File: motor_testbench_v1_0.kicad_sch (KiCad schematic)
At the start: 32 parts, among them IC1 PJA3402_R1_00001, J1 USB_C_Receptacle_USB2.0_16P, J2 Conn_01x22_Pin, J3 Conn_01x05_Pin, J4 Conn_01x01_Pin, J5 Conn_01x01_Pin, U1 ESP32-S3-WROOM-2, U2 ESP32-S3-DevKitC

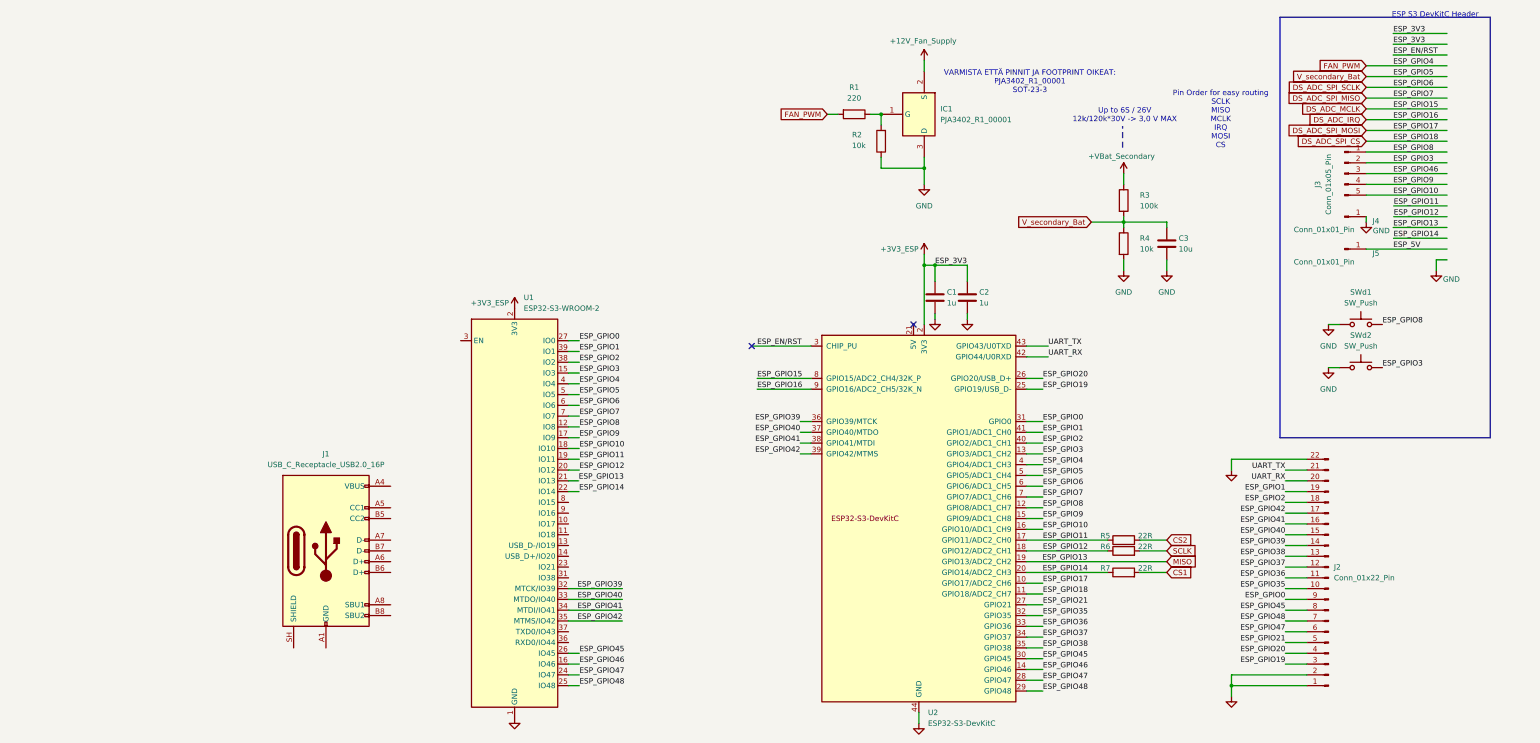
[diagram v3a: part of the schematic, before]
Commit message: Continue implementing ESP32 module
[KiCad Version: 10.0.3]
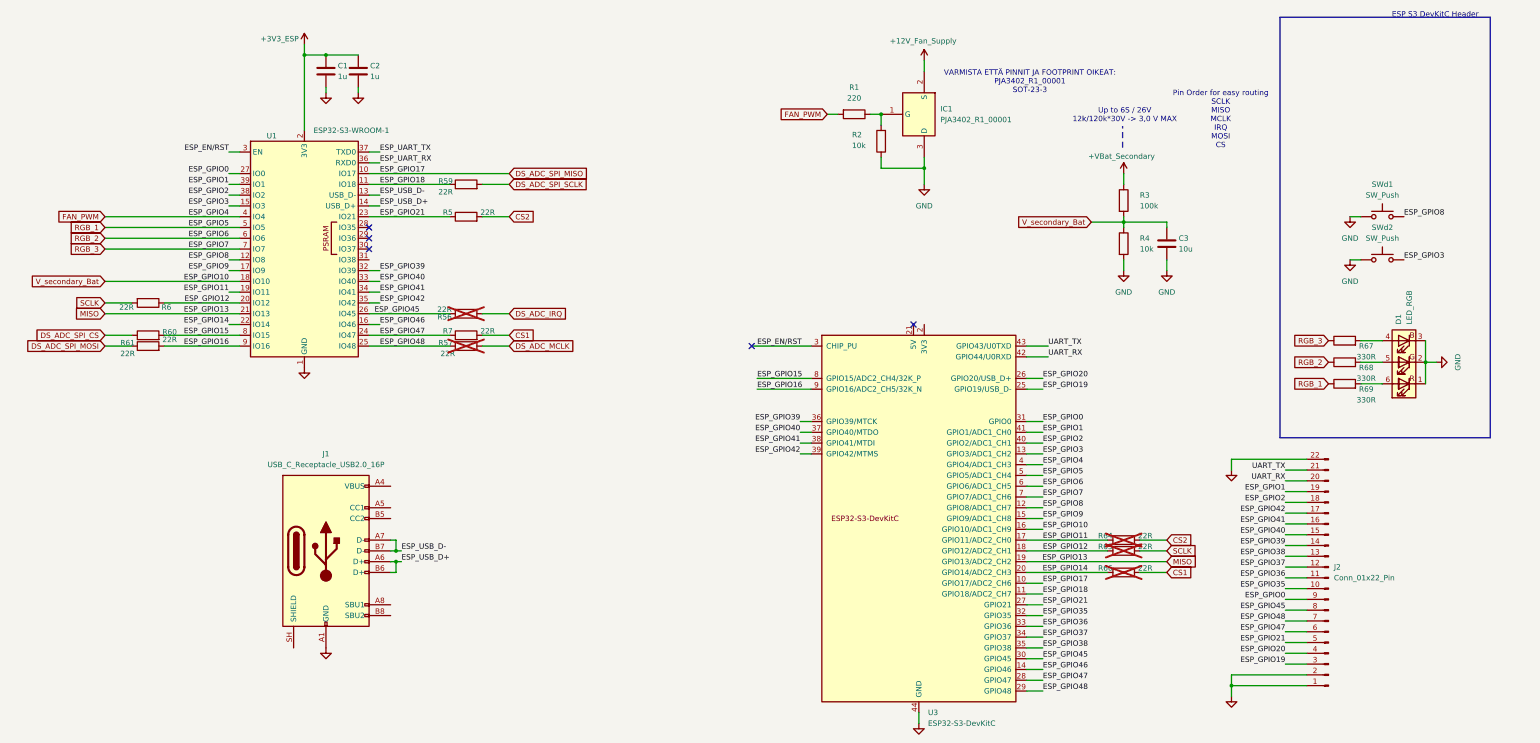
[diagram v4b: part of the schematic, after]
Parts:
- removed J3: Conn_01x05_Pin, Connector_PinHeader_2.54mm:PinHeader_1x05_P2.54mm_Vertical, symbol Connector:Conn_01x05_Pin
- removed J4, J5: Conn_01x01_Pin, Connector_PinHeader_2.54mm:PinHeader_1x01_P2.54mm_Vertical, symbol Connector:Conn_01x01_Pin
- removed U1: ESP32-S3-WROOM-2, RF_Module:ESP32-S3-WROOM-2, symbol RF_Module:ESP32-S3-WROOM-2
- added D1: LED_RGB, LED_SMD:LED_RGB_PLCC-6, symbol Device:LED_RGB
- added R56, R57, R59, R60, R61, R64, R65, R66: 22R, Resistor_SMD:R_0603_1608Metric_Pad0.98x0.95mm_HandSolder, symbol Device:R
- added R67, R68, R69: 330R, Resistor_SMD:R_0603_1608Metric_Pad0.98x0.95mm_HandSolder, symbol Device:R
- added U1: ESP32-S3-WROOM-1, RF_Module:ESP32-S3-WROOM-1, symbol RF_Module:ESP32-S3-WROOM-1
- renumbered U2 to U3
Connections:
- net ESP_GPIO10 is gone; now on net V_secondary_Bat: U3.16 (GPIO10/ADC1_CH9)
- net +3V3_ESP: now also U1.2 (3V3); no longer U3.1 (3V3), U3.2 (3V3)
- net CS1: now also R66.2
- net CS2: now also R64.2
- net DS_ADC_IRQ: now also R56.1; no longer U3.9 (GPIO16/ADC2_CH5/32K_N)
- net DS_ADC_MCLK: now also R57.2; no longer U3.8 (GPIO15/ADC2_CH4/32K_P)
- net DS_ADC_SPI_CS: now also R60.1; no longer U3.11 (GPIO18/ADC2_CH7)
- net DS_ADC_SPI_MISO: now also U3.10 (GPIO17/ADC2_CH6), U1.10 (IO17); no longer U3.7 (GPIO7/ADC1_CH6)
- net DS_ADC_SPI_MOSI: now also R61.1; no longer U3.10 (GPIO17/ADC2_CH6)
- net DS_ADC_SPI_SCLK: now also R59.2; no longer U3.6 (GPIO6/ADC1_CH5)
- net ESP_EN/RST: now also U1.3 (EN)
- net ESP_GPIO0: now also U1.27 (IO0)
- net ESP_GPIO1: now also U1.39 (IO1)
- net ESP_GPIO11: now also R64.1, U1.19 (IO11); no longer R5.1
- net ESP_GPIO12: now also R65.1, U1.20 (IO12)
- net ESP_GPIO14: now also R66.1, U1.22 (IO14); no longer R7.1
- net ESP_GPIO2: now also U1.38 (IO2)
- net ESP_GPIO21: now also R5.1, U1.23 (IO21)
- net ESP_GPIO3: now also U1.15 (IO3)
- net ESP_GPIO39: now also U1.32 (IO39)
- net ESP_GPIO40: now also U1.33 (IO40)
- net ESP_GPIO41: now also U1.34 (IO41)
- net ESP_GPIO42: now also U1.35 (IO42)
- net ESP_GPIO45: now also R56.2, U1.26 (IO45)
- net ESP_GPIO46: now also U1.16 (IO46)
- net ESP_GPIO47: now also R7.1, U1.24 (IO47)
- net ESP_GPIO48: now also R57.1, U1.25 (IO48)
- net ESP_GPIO8: now also U1.12 (IO8)
- net ESP_GPIO9: now also U1.17 (IO9)
- net FAN_PWM: now also U1.4 (IO4)
- net GND: now also J1.A1 (GND), J1.A12 (GND), J1.B1 (GND), J1.B12 (GND), D1.1 (RK), D1.2 (GK), D1.3 (BK), U1.1 (GND), U1.40 (GND), U1.41 (GND)
- net MISO: now also U1.21 (IO13)
- net SCLK: now also R65.2
- net V_secondary_Bat: now also U1.18 (IO10); no longer U3.5 (GPIO5/ADC1_CH4)
- net ESP_USB_D+: now reaches J1.A6 (D+)
- net ESP_USB_D+: now also J1.B6 (D+), U1.14 (USB_D+)
- net ESP_USB_D-: now reaches J1.A7 (D-)
- net ESP_USB_D-: now also J1.B7 (D-), U1.13 (USB_D-)
- new net: D1.6 (RA), R69.2
- new net: D1.5 (GA), R68.2
- new net: D1.4 (BA), R67.2
- new net: U3.1 (3V3), U3.2 (3V3)
- new net ESP_GPIO15: R60.2, U1.8 (IO15), U3.8 (GPIO15/ADC2_CH4/32K_P)
- new net ESP_GPIO16: R61.2, U1.9 (IO16), U3.9 (GPIO16/ADC2_CH5/32K_N)
- new net ESP_GPIO18: R59.1, U1.11 (IO18), U3.11 (GPIO18/ADC2_CH7)
- new net ESP_UART_RX: U1.36 (RXD0)
- new net ESP_UART_TX: U1.37 (TXD0)
- new net RGB_1: R69.1, U1.5 (IO5), U3.5 (GPIO5/ADC1_CH4)
- new net RGB_2: R68.1, U1.6 (IO6), U3.6 (GPIO6/ADC1_CH5)
- new net RGB_3: R67.1, U1.7 (IO7), U3.7 (GPIO7/ADC1_CH6)
- no-connect marks 2 -> 5
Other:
- moved on the sheet: SWd1, SWd2

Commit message: Add new GPIO header. Minor improvements.
[KiCad Version: 10.0.3]
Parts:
- removed J2: Conn_01x22_Pin, Connector_PinHeader_2.54mm:PinHeader_1x22_P2.54mm_Vertical, symbol Connector:Conn_01x22_Pin
- added J3: Conn_02x06_Odd_Even, Connector_PinHeader_2.00mm:PinHeader_2x06_P2.00mm_Vertical, symbol Connector_Generic:Conn_02x06_Odd_Even
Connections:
- net ESP_GPIO0: now also J3.3 (Pin_3)
- net ESP_GPIO1: now also J3.8 (Pin_8)
- net ESP_GPIO2: now also J3.10 (Pin_10)
- net ESP_GPIO38: now also U1.31 (IO38), J3.5 (Pin_5)
- net ESP_GPIO39: now also J3.7 (Pin_7)
- net ESP_GPIO40: now also J3.9 (Pin_9)
- net ESP_GPIO41: now also J3.11 (Pin_11)
- net ESP_GPIO42: now also J3.2 (Pin_2)
- net ESP_GPIO8: no longer SWd1.2
- net ESP_GPIO9: now also SWd1.2
- net ESP_UART_RX: now also J3.4 (Pin_4)
- net ESP_UART_TX: now also J3.6 (Pin_6)
- net GND: now also J3.1 (Pin_1), J3.12 (Pin_12)
- net V_secondary_Bat: now also U1.15 (IO3), U3.13 (GPIO3/ADC1_CH2); no longer U1.18 (IO10), U3.16 (GPIO10/ADC1_CH9)
- removed net ESP_GPIO3: SWd2.2, U1.15 (IO3), U3.13 (GPIO3/ADC1_CH2)
- new net ESP_GPIO10: SWd2.2, U1.18 (IO10), U3.16 (GPIO10/ADC1_CH9)
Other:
- note removed: "Pin Order for easy routing SCLK MISO MCLK IRQ MOSI CS"
- moved on the sheet: C1, C2, D1, J1, R5, R56, R57, R59, R6, R60, R61, R67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
